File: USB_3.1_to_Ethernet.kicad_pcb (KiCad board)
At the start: 4 copper layers, 75 x 25 mm, 93 parts, among them J1 RJ45_JK0654219, J2 USB3_A, U1 LAN7801_9JX, U2 93LC56B_SN, U3 KSZ9031RNXCC, U4 TLV76733, U5 USBLC6-2P6, U6 TPS7A0212, Y1 25MHz, Y2 25MHz

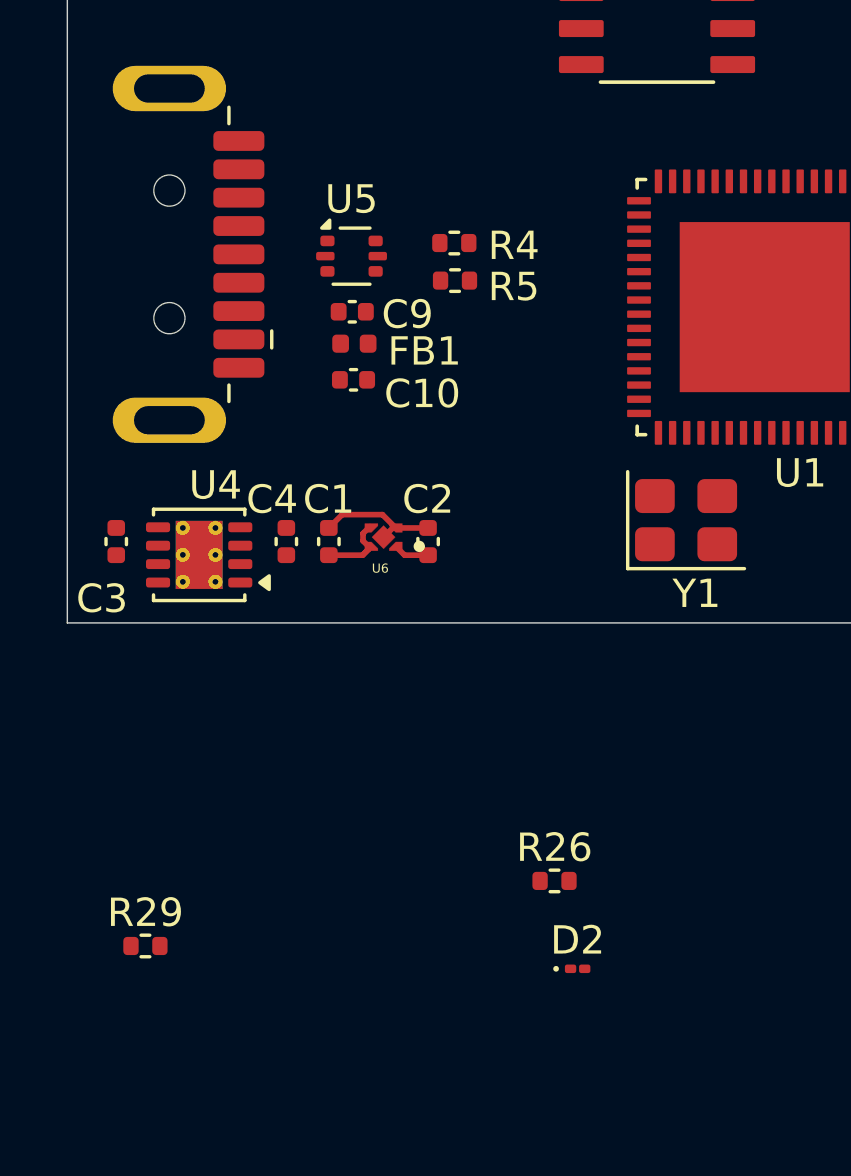
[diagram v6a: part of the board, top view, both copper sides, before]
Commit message: 1. net class assigned to all the nets 2.Slight placement changes
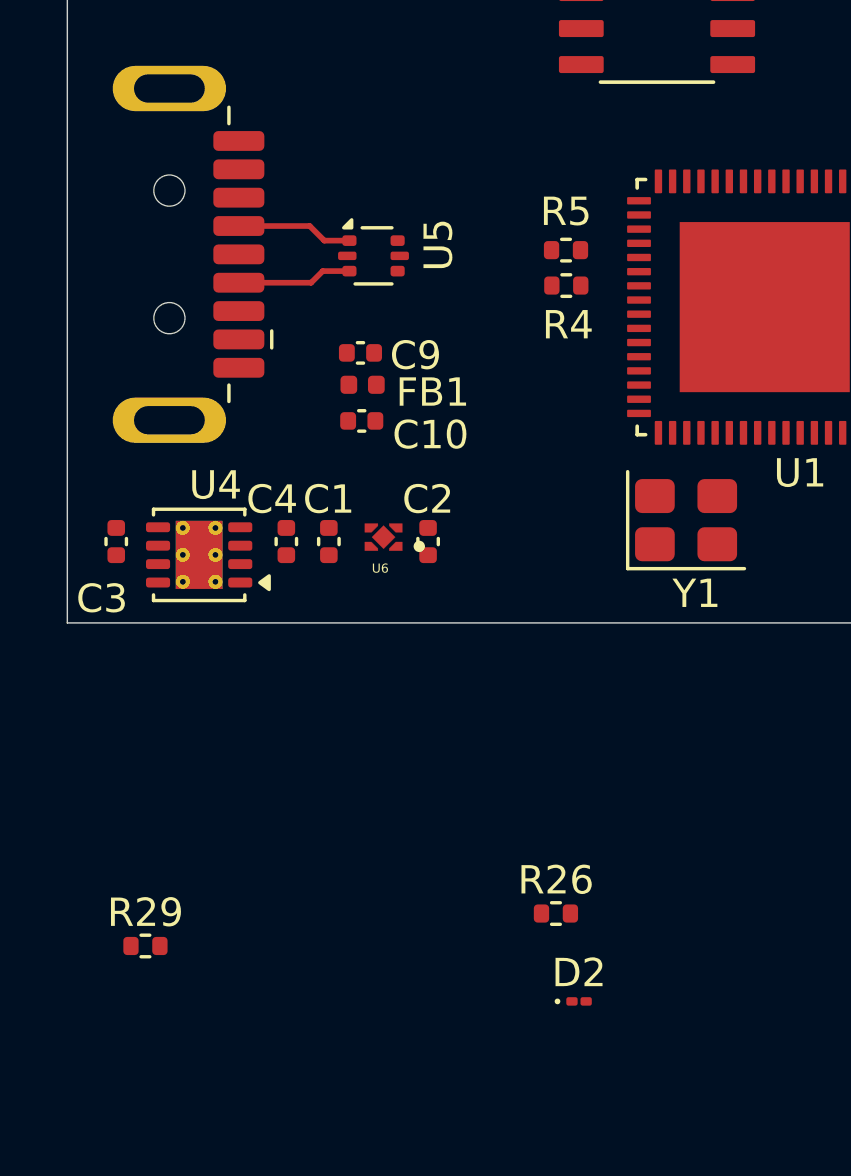
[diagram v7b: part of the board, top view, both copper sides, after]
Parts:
- moved R4 4.23 mm to (77.3, 63.2)
- moved R5 4.06 mm to (77.3, 62.0)
- moved C9 1.48 mm to (70.0, 65.6)
- moved FB1 1.48 mm to (70.1, 66.7)
- moved C10 1.48 mm to (70.1, 68.0)
- moved D2 1.15 mm to (77.8, 88.5)
- moved R26 1.15 mm to (76.9, 85.3)
- moved U5 0.78 mm to (70.5, 62.2)
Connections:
- net Net-(R4-Pad1) renamed /Power section/_P
- net Net-(R5-Pad1) renamed /Power section/_N
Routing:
- net GND: track 4.45 -> 0.00 mm
- net /Power section/DN: track 0.00 -> 4.11 mm
- net /Power section/DP: track 0.00 -> 4.07 mm
- net 3v3_out: track 2.84 -> 0.00 mm
- net 1v2_core: track 1.20 -> 0.00 mm
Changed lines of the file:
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@@
 		(capping no)
 		(filling no)
+		(zone_defaults)
 		(pcbplotparams
 			(layerselection 0x00000000_00000000_55555555_5755f5ff)
@@
 	(footprint "Capacitor_SMD:C_0402_1005Metric"
 		(layer "F.Cu")
-		(at 69.75 64.125)
+		(at 70.04 65.575)
 		(descr "Capacitor SMD 0402 (1005 Metric), square (rectangular) end terminal, IPC-7351 nominal, (Body size source: IPC-SM-782 page 76, https://www.pcb-3d.com/wordpress/wp-content/uploads/ipc-sm-782a_amendment_1_and_2.pdf)")
 		(tags "capacitor")
@@
 	(footprint "Resistor_SMD:R_0402_1005Metric"
 		(layer "F.Cu")
-		(at 73.375 63.025)
+		(at 77.29 61.95)
 		(descr "Resistor SMD 0402 (1005 Metric), square (rectangular) end terminal, IPC-7351 nominal, (Body size source: IPC-SM-782 page 72, https://www.pcb-3d.com/wordpress/wp-content/uploads/ipc-sm-782a_amendment_1_and_2.pdf)")
 		(tags "resistor")
 		(property "Reference" "R5"
-			(at 2.075 0.225 180)
+			(at 0 -1.35 180)
 			(layer "F.SilkS")
 			(effects
@@
 			(layers "F.Cu" "F.Mask" "F.Paste")
 			(roundrect_rratio 0.25)
-			(net "Net-(R5-Pad1)")
+			(net "/Power section/_N")
 			(pintype "passive")
 		)
@@
 	(footprint "Resistor_SMD:R_0402_1005Metric"
 		(layer "F.Cu")
-		(at 76.885 84.2)
+		(at 76.935 85.35)
 		(descr "Resistor SMD 0402 (1005 Metric), square (rectangular) end terminal, IPC-7351 nominal, (Body size source: IPC-SM-782 page 72, https://www.pcb-3d.com/wordpress/wp-content/uploads/ipc-sm-782a_amendment_1_and_2.pdf)")
 		(tags "resistor")
@@
 	(footprint "LED_SMD:LED_01005_0402Metric"
 		(layer "F.Cu")
-		(at 77.7 87.3)
+		(at 77.75 88.45)
 		(descr "LED SMD 01005 (0402 Metric), square (rectangular) end terminal, IPC-7351 nominal, (Body size source: http://www.vishay.com/docs/20056/crcw01005e3.pdf)")
 		(tags "LED")
@@
 	(footprint "Resistor_SMD:R_0402_1005Metric"
 		(layer "F.Cu")
-		(at 73.35 61.7)
+		(at 77.3 63.2)
 		(descr "Resistor SMD 0402 (1005 Metric), square (rectangular) end terminal, IPC-7351 nominal, (Body size source: IPC-SM-782 page 72, https://www.pcb-3d.com/wordpress/wp-content/uploads/ipc-sm-782a_amendment_1_and_2.pdf)")
 		(tags "resistor")
 		(property "Reference" "R4"
-			(at 2.1 0.1 180)
+			(at 0.06 1.4 180)
 			(layer "F.SilkS")
 			(effects
@@
 			(layers "F.Cu" "F.Mask" "F.Paste")
 			(roundrect_rratio 0.25)
-			(net "Net-(R4-Pad1)")
+			(net "/Power section/_P")
 			(pintype "passive")
 		)
@@
 	(footprint "Inductor_SMD:L_0402_1005Metric"
 		(layer "F.Cu")
-		(at 69.825 65.25)
+		(at 70.115 66.7)
 		(descr "Inductor SMD 0402 (1005 Metric), square (rectangular) end terminal, IPC-7351 nominal, (Body size source: http://www.tortai-tech.com/upload/download/2011102023233369053.pdf)")
 		(tags "inductor")
@@
 	(footprint "Package_TO_SOT_SMD:SOT-666"
 		(layer "F.Cu")
-		(at 69.725 62.1625)
+		(at 70.5 62.1525)
 		(descr "SOT666")
 		(tags "SOT-666")
 		(property "Reference" "U5"
-			(at 0 -2 0)
+			(at 2.3 -0.3875 90)
 			(layer "F.SilkS")
 			(effects
@@
 			(layers "F.Cu" "F.Mask" "F.Paste")
 			(roundrect_rratio 0.25)
-			(net "Net-(R5-Pad1)")
+			(net "/Power section/_N")
 			(pinfunction "I/O2_4")
 			(pintype "passive")
@@
 			(layers "F.Cu" "F.Mask" "F.Paste")
 			(roundrect_rratio 0.25)
-			(net "Net-(R4-Pad1)")
+			(net "/Power section/_P")
 			(pinfunction "I/O1_6")
 			(pintype "passive")
@@
 	(footprint "Capacitor_SMD:C_0402_1005Metric"
 		(layer "F.Cu")
-		(at 69.795 66.525)
+		(at 70.085 67.975)
 		(descr "Capacitor SMD 0402 (1005 Metric), square (rectangular) end terminal, IPC-7351 nominal, (Body size source: IPC-SM-782 page 76, https://www.pcb-3d.com/wordpress/wp-content/uploads/ipc-sm-782a_amendment_1_and_2.pdf)")
 		(tags "capacitor")
@@
 	)
 	(segment
-		(start 68.925 71.75)
-		(end 69.395 71.28)
+		(start 65.75 63.1)
+		(end 68.3 63.1)
 		(width 0.2)
 		(layer "F.Cu")
-		(net "GND")
+		(net "/Power section/DP")
 	)
 	(segment
-		(start 69.395 71.28)
-		(end 70.815 71.28)
+		(start 68.71 62.69)
+		(end 69.65 62.69)
 		(width 0.2)
 		(layer "F.Cu")
-		(net "GND")
+		(net "/Power section/DP")
 	)
 	(segment
-		(start 70.815 71.28)
-		(end 71.285 71.75)
+		(start 68.3 63.1)
+		(end 68.71 62.69)
 		(width 0.2)
 		(layer "F.Cu")
-		(net "GND")
+		(net "/Power section/DP")
 	)
 	(segment
-		(start 71.285 71.75)
-		(end 71.18 71.75)
+		(start 68.765 61.615)
+		(end 69.65 61.615)
 		(width 0.2)
 		(layer "F.Cu")
-		(net "GND")
+		(net "/Power section/DN")
 	)
 	(segment
-		(start 71.18 71.75)
-		(end 70.855 72.075)
+		(start 65.75 61.1)
+		(end 68.25 61.1)
 		(width 0.2)
 		(layer "F.Cu")
-		(net "GND")
+		(net "/Power section/DN")
 	)
 	(segment
-		(start 71.285 71.75)
-		(end 72.425 71.75)
+		(start 68.25 61.1)
+		(end 68.765 61.615)
 		(width 0.2)
 		(layer "F.Cu")
-		(net "GND")
-	)
-	(segment
-		(start 72.425 72.71)
-		(end 71.595 72.71)
-		(width 0.2)
-		(layer "F.Cu")
-		(net "1v2_core")
-	)
-	(segment
-		(start 71.595 72.71)
-		(end 71.335302 72.450302)
-		(width 0.2)
-		(layer "F.Cu")
-		(net "1v2_core")
-	)
-	(segment
-		(start 70.324398 72.4)
-		(end 70.130259 72.205861)
-		(width 0.2)
-		(layer "F.Cu")
-		(net "3v3_out")
-	)
-	(segment
-		(start 70.115 72.71)
-		(end 70.374699 72.450301)
-		(width 0.2)
-		(layer "F.Cu")
-		(net "3v3_out")
-	)
-	(segment
-		(start 70.324398 72.500602)
-		(end 70.324398 72.4)
-		(width 0.2)
-		(layer "F.Cu")
-		(net "3v3_out")
-	)
-	(segment
-		(start 68.925 72.71)
-		(end 70.115 72.71)
-		(width 0.2)
-		(layer "F.Cu")
-		(net "3v3_out")
-	)
-	(segment
-		(start 70.130259 72.205861)
-		(end 70.130259 71.944139)
-		(width 0.2)
-		(layer "F.Cu")
-		(net "3v3_out")
-	)
-	(segment
-		(start 70.115 72.71)
-		(end 70.324398 72.500602)
-		(width 0.2)
-		(layer "F.Cu")
-		(net "3v3_out")
-	)
-	(segment
-		(start 70.130259 71.944139)
-		(end 70.374699 71.699699)
-		(width 0.2)
-		(layer "F.Cu")
-		(net "3v3_out")
+		(net "/Power section/DN")
 	)
 	(group ""
 		(members "40f13ff6-3ea6-4880-a3e4-f48974f515e7" "621548ba-3899-4c50-8ae5-d07bf10f0522")
 	)
-	(group ""
-		(members "06db212b-1de4-4a90-9a68-9a6e5fc0516d" "0784a02c-ed79-4100-a4fc-001d9f5013b3"
-			"0e86d0b1-b389-4de3-bc8a-e04a2b013484" "19687c95-bbf2-47aa-88c5-137dbd08ef06"
-			"1f3faeb6-acfc-45c1-9002-2c686d975e55" "2afabf4c-d650-44db-9939-ad48bfa3c309"
-			"3222601d-b325-4e51-b9d4-b3bde82452cc" "3d1d58ed-5b74-41dd-89ac-a44b6c826302"
-			"56dcd77c-833f-4ab0-bc9b-f601eee5581f" "65ec8262-dedc-4a6b-b48f-ec17251e2615"
-			"6d70a0f1-dea0-407d-bdbb-cb8c4fef35ba" "7c6b2208-8fe0-433e-a3b9-a925f649f22a"
-			"83a7efcb-e7e3-4252-9acc-546129fb6f57" "8f20b012-3f6f-47de-b97f-bd2307546683"
-			"923fae6b-566a-4c99-a54d-8d355ab82297" "9d6defd6-b804-4fe9-acb3-aff328cf5347"
-			"bae0b8d2-5acd-4288-9b57-7e519fbaf4c1" "bbd66c82-8a69-4dfe-b953-ffd9edb33946"
-			"d18ed461-aa78-4aad-81d4-486c4ee88a63" "d2edf608-30e4-4c12-a1d0-88a50ee61f02"
-			"fc77f879-fbf7-458f-bc0b-995563041cbb"
-		)
-	)
 	(embedded_fonts no)

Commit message: 1. Major routing done- usb3.1,usb2, >> 2. buck converter and voltage regulators placement and routing done >> 3. Decoupling caps added
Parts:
- C1, C2, C3, C4, FB1, U4, U6: moved to B.Cu
- moved C34 93.2 mm to (77.3, 65.3), turned to 180 degrees
- moved C29 92.8 mm to (78.0, 59.9), turned to 90 degrees
- moved C27 81.7 mm to (88.3, 71.2)
- moved R22 77.3 mm to (77.3, 68.6)
- moved C12 71.3 mm to (77.0, 63.5)
- moved C11 68.2 mm to (77.0, 64.4)
- moved R28 32.9 mm to (76.6, 67.4), turned to 180 degrees
- moved R29 32.6 mm to (78.7, 58.2), turned to 90 degrees
- moved FB1 7.63 mm to (62.5, 66.1), turned to 180 degrees
- moved C2 5.54 mm to (67.8, 69.2), turned to 0 degrees
- moved U6 3.34 mm to (67.7, 71.0), turned to -90 degrees
- moved C10 2.56 mm to (68.8, 65.7)
- moved C1 2.14 mm to (67.0, 73.1), turned to -90 degrees
- moved C9 1.57 mm to (68.8, 64.6)
- moved R4 1.42 mm to (76.5, 62.0)
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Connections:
- C10 pad 2: SSTX+ -> SSRX-
- C11 pad 2: SSRX+ -> SSTX-
- C12 pad 2: SSRX- -> SSTX+
- C9 pad 2: SSTX- -> SSRX+
- J2 pad 2: /Power section/DP -> /Power section/DN
- J2 pad 3: /Power section/DN -> /Power section/DP
- U5 pad 1: /Power section/DN -> /Power section/DP
- U5 pad 3: /Power section/DP -> /Power section/DN
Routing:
- net /Power section/ssrx_P: track 0.00 -> 13.1 mm
- net /Power section/ssrx_N: track 0.00 -> 13.0 mm
- net GND: track 0.00 -> 12.8 mm
- net SSRX+: track 0.00 -> 11.7 mm
- net SSRX-: track 0.00 -> 11.4 mm
- net /Power section/_P: track 0.00 -> 9.55 mm, vias 0 -> 2
- net /Power section/_N: track 0.00 -> 6.68 mm, vias 0 -> 2
- net 1v2_core: track 0.00 -> 5.81 mm, vias 0 -> 2
- net 3v3_out: track 0.00 -> 3.95 mm
- net Net-(U1-PME_MODE/GPIO5): track 0.00 -> 3.85 mm
- net D+: track 0.00 -> 3.63 mm
- net D-: track 0.00 -> 3.36 mm
- net Net-(U1-~{PME_N}/GPIO6): track 0.00 -> 3.22 mm
- net VBUS: track 0.00 -> 3.17 mm, vias 0 -> 1
- net /Power section/sstx_N: track 0.00 -> 2.84 mm
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- added copper zone on B.Cu, net +5V
- added copper zone on B.Cu, net 3v3_out
